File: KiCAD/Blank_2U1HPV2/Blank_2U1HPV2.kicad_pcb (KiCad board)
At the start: 2 copper layers, 5 x 84 mm, 2 parts

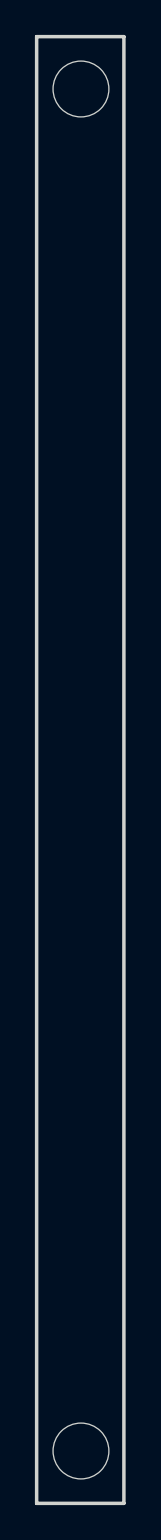
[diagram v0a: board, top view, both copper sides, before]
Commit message: updated all modules to use plated through-holes wherever possible
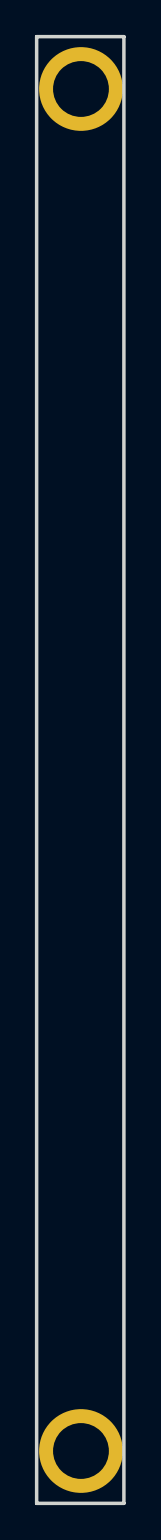
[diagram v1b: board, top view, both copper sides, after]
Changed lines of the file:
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@@
 			)
 		)
-		(pad "" np_thru_hole circle
+		(pad "" thru_hole circle
 			(at 0 0)
-			(size 3.2 3.2)
+			(size 4.8 4.8)
 			(drill 3.2)
 			(layers "*.Cu" "*.Mask")
+			(remove_unused_layers no)
 		)
 		(embedded_fonts no)
@@
 			)
 		)
-		(pad "" np_thru_hole circle
+		(pad "" thru_hole circle
 			(at 0 0)
-			(size 3.2 3.2)
+			(size 4.8 4.8)
 			(drill 3.2)
 			(layers "*.Cu" "*.Mask")
+			(remove_unused_layers no)
 		)
 		(embedded_fonts no)
